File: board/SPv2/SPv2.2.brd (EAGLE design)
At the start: 56.5 x 22.9 mm, 39 parts, among them IC1 S34ML0XG1, IC2 F5508, IC4 74LS14DB, Q1 12MHz

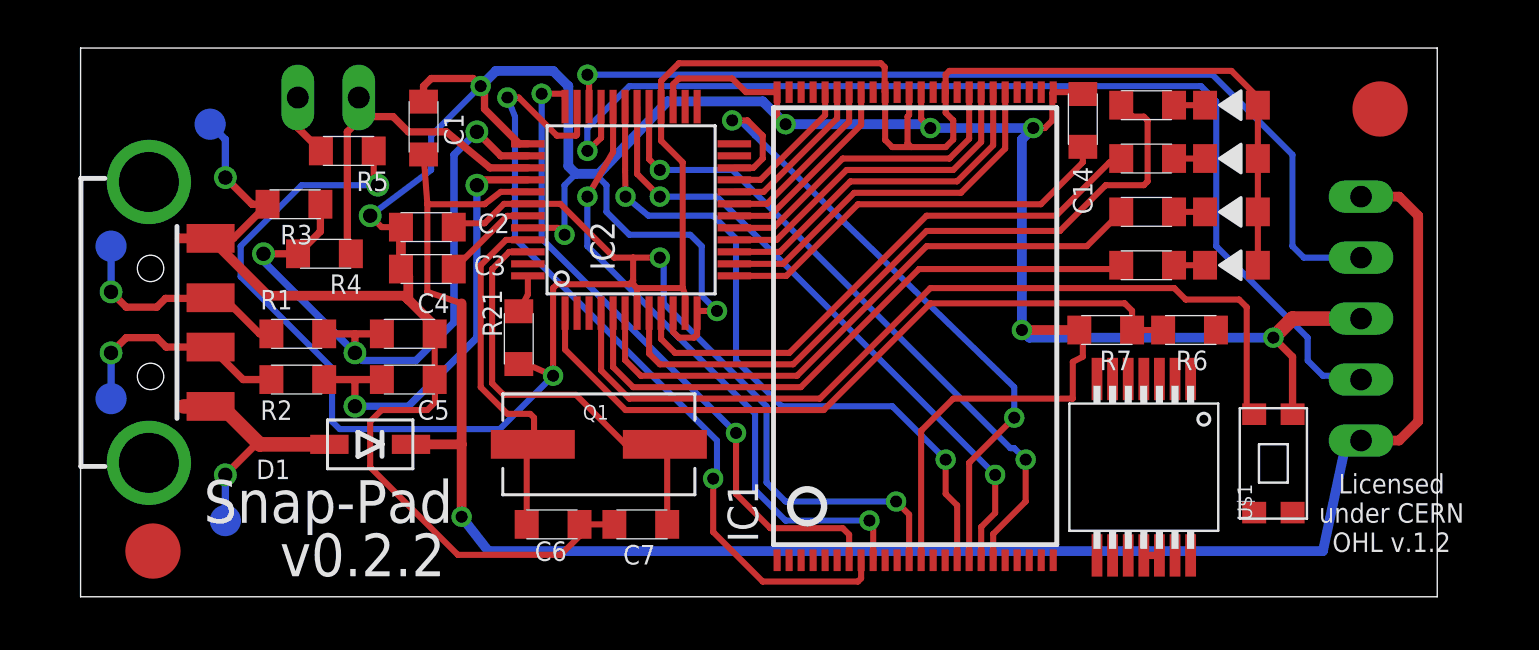
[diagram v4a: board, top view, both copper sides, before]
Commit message: test pads in, routing finalized
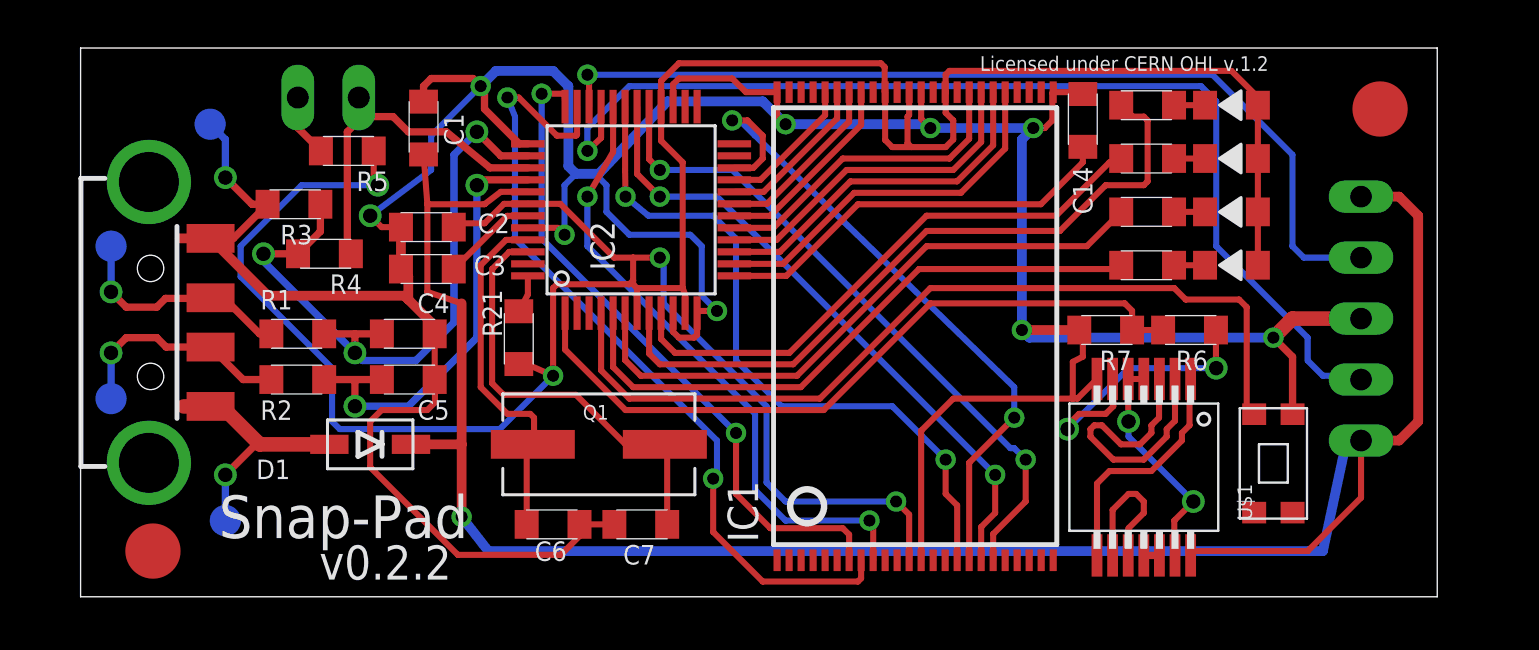
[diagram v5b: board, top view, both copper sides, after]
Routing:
- net N$10: track 0.00 -> 12.4 mm, vias 0 -> 2
- net N$8: track 0.00 -> 12.3 mm
- net VBUS: track 78.4 -> 88.8 mm
- net N$7: track 0.00 -> 9.99 mm
- net N$9: track 0.00 -> 9.47 mm, vias 0 -> 2
- net N$6: track 0.00 -> 6.12 mm
- net GND: track 162.2 -> 163.6 mm
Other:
- board text added: "(c)2014-5 phooky"
- board text removed: "(c) 2014 phooky Licensed under CERN OHL v.1.2"
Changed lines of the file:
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@@
 <wire x1="57.785" y1="22.86" x2="1.27" y2="22.86" width="0" layer="20"/>
 <wire x1="1.27" y1="22.86" x2="1.27" y2="0" width="0" layer="20"/>
-<text x="11.58875" y="3.96875" size="1.778" layer="21" font="vector" ratio="12" align="center">Snap-Pad</text>
-<text x="13.0175" y="1.74625" size="1.778" layer="21" font="vector" ratio="12" align="center">v0.2.2</text>
-<text x="55.88" y="3.4925" size="0.8128" layer="21" font="vector" ratio="12" align="center">Licensed
-under CERN
-OHL v.1.2</text>
-<text x="42.545" y="2.06375" size="0.6096" layer="22" font="vector" ratio="12" rot="MR0" align="center">(c) 2014 phooky
-Licensed under CERN OHL v.1.2</text>
+<text x="12.22375" y="3.33375" size="1.778" layer="21" font="vector" ratio="12" align="center">Snap-Pad</text>
+<text x="13.97" y="1.42875" size="1.4224" layer="21" font="vector" ratio="12" align="center">v0.2.2</text>
 <text x="42.06875" y="14.605" size="1.016" layer="22" font="vector" ratio="12" rot="MR0" align="center">Documentation, sources and
 more can be found at:
 http://snap-pad.info/
 </text>
+<text x="27.6225" y="0.635" size="1.016" layer="22" font="vector" ratio="12" rot="MR20">Licensed under
+CERN OHL v.1.2</text>
+<text x="43.18" y="0.9525" size="1.016" layer="22" font="vector" ratio="12" rot="MR0">(c)2014-5 phooky</text>
+<text x="38.735" y="21.9075" size="0.6096" layer="21" font="vector" ratio="12">Licensed under CERN OHL v.1.2</text>
 </plain>
 <attributes>
@@
 </autorouter>
 <elements>
-<element name="IC1" library="Flash" package="TSOP48" value="S34ML0XG1" x="36.03625" y="11.27125" rot="R90"/>
+<element name="IC1" library="Flash" package="TSOP48" value="S34ML0XG1" x="36.03625" y="11.27125" smashed="yes" rot="R90">
+<attribute name="NAME" x="29.49625" y="2.27125" size="1.27" layer="25" font="vector" rot="R90"/>
+<attribute name="VALUE" x="36.57625" y="6.77125" size="1.27" layer="27" rot="R90"/>
+</element>
 <element name="IC2" library="TI_MSP430_v16" package="PT48" value="F5508" x="24.20373125" y="16.118765625" smashed="yes" rot="R90">
 <attribute name="VALUE" x="27.33873125" y="13.753765625" size="1.016" layer="27" ratio="10" rot="R90"/>
@@
 <wire x1="51.75875" y1="7.60625" x2="51.75875" y2="9.995" width="0.3048" layer="1"/>
 <wire x1="51.75875" y1="9.995" x2="50.95875" y2="10.795" width="0.3048" layer="1"/>
-<wire x1="43.02125" y1="10.00125" x2="43.61125" y2="9.0725" width="0" layer="19" extent="1-1"/>
+<wire x1="43.61125" y1="9.0725" x2="42.79375" y2="8.255" width="0.254" layer="1"/>
+<wire x1="42.79375" y1="8.255" x2="42.60215" y2="8.255" width="0.254" layer="1"/>
 </signal>
 <signal name="+3V3_A">
@@
 <wire x1="15.71625" y1="16.35125" x2="15.71625" y2="16.3625" width="0.254" layer="1"/>
 <wire x1="15.71625" y1="16.3625" x2="15.5575" y2="18.42625" width="0.254" layer="1"/>
-<wire x1="53.0225" y1="1.905" x2="47.51125" y2="1.7225" width="0" layer="19" extent="1-16"/>
+<wire x1="47.51125" y1="1.7225" x2="47.69375" y2="1.905" width="0.254" layer="1"/>
+<wire x1="47.69375" y1="1.905" x2="52.3875" y2="1.905" width="0.254" layer="1"/>
+<wire x1="52.3875" y1="1.905" x2="54.61" y2="4.1275" width="0.254" layer="1"/>
+<wire x1="54.61" y1="4.1275" x2="54.61" y2="6.50875" width="0.254" layer="1"/>
 </signal>
 <signal name="+1V8_A">
@@
 <contactref element="IC4" pad="10"/>
 <contactref element="IC4" pad="9"/>
-<wire x1="44.26125" y1="1.7225" x2="44.91125" y2="1.7225" width="0" layer="19" extent="1-1"/>
+<wire x1="44.91125" y1="1.7225" x2="44.92625" y2="1.7375" width="0.254" layer="1"/>
+<wire x1="44.92625" y1="1.7375" x2="44.92625" y2="2.8575" width="0.254" layer="1"/>
+<wire x1="44.92625" y1="2.8575" x2="45.56125" y2="3.4925" width="0.254" layer="1"/>
+<wire x1="45.56125" y1="3.4925" x2="45.56125" y2="3.96875" width="0.254" layer="1"/>
+<wire x1="45.56125" y1="3.96875" x2="45.24375" y2="4.28625" width="0.254" layer="1"/>
+<wire x1="45.24375" y1="4.28625" x2="44.92625" y2="4.28625" width="0.254" layer="1"/>
+<wire x1="44.92625" y1="4.28625" x2="44.26125" y2="3.62125" width="0.254" layer="1"/>
+<wire x1="44.26125" y1="3.62125" x2="44.26125" y2="1.7225" width="0.254" layer="1"/>
 </signal>
 <signal name="N$7">
 <contactref element="IC4" pad="8"/>
 <contactref element="IC4" pad="1"/>
-<wire x1="43.61125" y1="1.7225" x2="47.51125" y2="9.0725" width="0" layer="19" extent="1-1"/>
+<wire x1="47.51125" y1="9.0725" x2="47.46625" y2="9.0275" width="0.254" layer="1"/>
+<wire x1="47.46625" y1="9.0275" x2="47.46625" y2="7.14375" width="0.254" layer="1"/>
+<wire x1="47.46625" y1="7.14375" x2="47.14875" y2="6.82625" width="0.254" layer="1"/>
+<wire x1="47.14875" y1="6.82625" x2="47.14875" y2="6.50875" width="0.254" layer="1"/>
+<wire x1="47.14875" y1="6.50875" x2="45.87875" y2="5.23875" width="0.254" layer="1"/>
+<wire x1="45.87875" y1="5.23875" x2="44.1325" y2="5.23875" width="0.254" layer="1"/>
+<wire x1="44.1325" y1="5.23875" x2="43.61125" y2="4.7175" width="0.254" layer="1"/>
+<wire x1="43.61125" y1="4.7175" x2="43.61125" y2="1.7225" width="0.254" layer="1"/>
 </signal>
 <signal name="N$8">
 <contactref element="IC4" pad="2"/>
 <contactref element="IC4" pad="3"/>
-<wire x1="46.21125" y1="9.0725" x2="46.86125" y2="9.0725" width="0" layer="19" extent="1-1"/>
+<wire x1="46.21125" y1="9.0725" x2="46.19625" y2="9.0575" width="0.254" layer="1"/>
+<wire x1="46.19625" y1="9.0575" x2="46.19625" y2="7.46125" width="0.254" layer="1"/>
+<wire x1="46.19625" y1="7.46125" x2="45.87875" y2="7.14375" width="0.254" layer="1"/>
+<wire x1="45.87875" y1="7.14375" x2="45.87875" y2="6.82625" width="0.254" layer="1"/>
+<wire x1="45.87875" y1="6.82625" x2="45.4025" y2="6.35" width="0.254" layer="1"/>
+<wire x1="45.4025" y1="6.35" x2="44.60875" y2="6.35" width="0.254" layer="1"/>
+<wire x1="44.60875" y1="6.35" x2="43.815" y2="7.14375" width="0.254" layer="1"/>
+<wire x1="43.815" y1="7.14375" x2="43.4975" y2="7.14375" width="0.254" layer="1"/>
+<wire x1="43.4975" y1="7.14375" x2="43.33875" y2="6.985" width="0.254" layer="1"/>
+<wire x1="43.33875" y1="6.985" x2="43.33875" y2="6.6675" width="0.254" layer="1"/>
+<wire x1="43.33875" y1="6.6675" x2="44.29125" y2="5.715" width="0.254" layer="1"/>
+<wire x1="44.29125" y1="5.715" x2="45.56125" y2="5.715" width="0.254" layer="1"/>
+<wire x1="45.56125" y1="5.715" x2="46.51375" y2="6.6675" width="0.254" layer="1"/>
+<wire x1="46.51375" y1="6.6675" x2="46.51375" y2="6.985" width="0.254" layer="1"/>
+<wire x1="46.51375" y1="6.985" x2="46.86125" y2="7.3325" width="0.254" layer="1"/>
+<wire x1="46.86125" y1="7.3325" x2="46.86125" y2="9.0725" width="0.254" layer="1"/>
 </signal>
 <signal name="N$9">
@@
 <contactref element="IC4" pad="13"/>
 <contactref element="IC4" pad="5"/>
-<wire x1="44.91125" y1="9.0725" x2="45.56125" y2="9.0725" width="0" layer="19" extent="1-1"/>
-<wire x1="46.86125" y1="1.7225" x2="45.56125" y2="9.0725" width="0" layer="19" extent="1-1"/>
+<wire x1="46.86125" y1="1.7225" x2="46.83125" y2="1.7525" width="0.254" layer="1"/>
+<wire x1="46.83125" y1="1.7525" x2="46.83125" y2="3.175" width="0.254" layer="1"/>
+<wire x1="46.83125" y1="3.175" x2="47.625" y2="3.96875" width="0.254" layer="1"/>
+<via x="47.625" y="3.96875" extent="1-16" drill="0.6"/>
+<wire x1="47.625" y1="3.96875" x2="44.92625" y2="6.6675" width="0.254" layer="16"/>
+<wire x1="44.92625" y1="6.6675" x2="44.92625" y2="7.3025" width="0.254" layer="16"/>
+<via x="44.92625" y="7.3025" extent="1-16" drill="0.6"/>
+<wire x1="44.92625" y1="7.3025" x2="44.91125" y2="7.3175" width="0.254" layer="1"/>
+<wire x1="44.91125" y1="7.3175" x2="44.91125" y2="9.0725" width="0.254" layer="1"/>
+<wire x1="44.91125" y1="9.0725" x2="45.56125" y2="9.0725" width="0.254" layer="1"/>
 </signal>
 <signal name="N$10">
 <contactref element="IC4" pad="6"/>
 <contactref element="R6" pad="P$2"/>
-<wire x1="44.26125" y1="9.0725" x2="48.56625" y2="11.1125" width="0" layer="19" extent="1-1"/>
+<wire x1="44.26125" y1="9.0725" x2="44.29125" y2="9.0425" width="0.254" layer="1"/>
+<wire x1="44.29125" y1="9.0425" x2="44.29125" y2="7.9375" width="0.254" layer="1"/>
+<wire x1="44.29125" y1="7.9375" x2="43.97375" y2="7.62" width="0.254" layer="1"/>
+<wire x1="43.97375" y1="7.62" x2="42.8625" y2="7.62" width="0.254" layer="1"/>
+<wire x1="42.8625" y1="7.62" x2="42.38625" y2="7.14375" width="0.254" layer="1"/>
+<wire x1="42.38625" y1="7.14375" x2="42.38625" y2="6.985" width="0.254" layer="1"/>
+<via x="42.38625" y="6.985" extent="1-16" drill="0.6"/>
+<wire x1="42.38625" y1="6.985" x2="44.92625" y2="9.525" width="0.254" layer="16"/>
+<wire x1="44.92625" y1="9.525" x2="48.5775" y2="9.525" width="0.254" layer="16"/>
+<via x="48.5775" y="9.525" extent="1-16" drill="0.6"/>
+<wire x1="48.5775" y1="9.525" x2="48.56625" y2="9.53625" width="0.254" layer="1"/>
+<wire x1="48.56625" y1="9.53625" x2="48.56625" y2="11.1125" width="0.254" layer="1"/>
 </signal>
 </signals>
